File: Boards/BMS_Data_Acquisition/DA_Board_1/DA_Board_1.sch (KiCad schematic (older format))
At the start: 75 parts, among them J1 MM_M_VT_10, J2 MM_M_VT_12, J3 MM_M_VT_12, J4 MM_M_VT_12, J5 MM_M_VT_16, J6 MM_M_VT_10, J7 MM_M_VT_12, J8 MM_M_VT_12, J9 MM_M_VT_12, Q10 BSS308PE, Q12 BSS308PE, Q14 BSS308PE, Q16 BSS308PE, Q2 BSS308PE, Q4 BSS308PE, Q6 BSS308PE, Q8 BSS308PE, T0 Tab_Connect_BMS, T10 Tab_Connect_BMS, T12 Tab_Connect_BMS, T14 Tab_Connect_BMS, T16 Tab_Connect_BMS, T2 Tab_Connect_BMS, T4 Tab_Connect_BMS, T6 Tab_Connect_BMS, T8 Tab_Connect_BMS

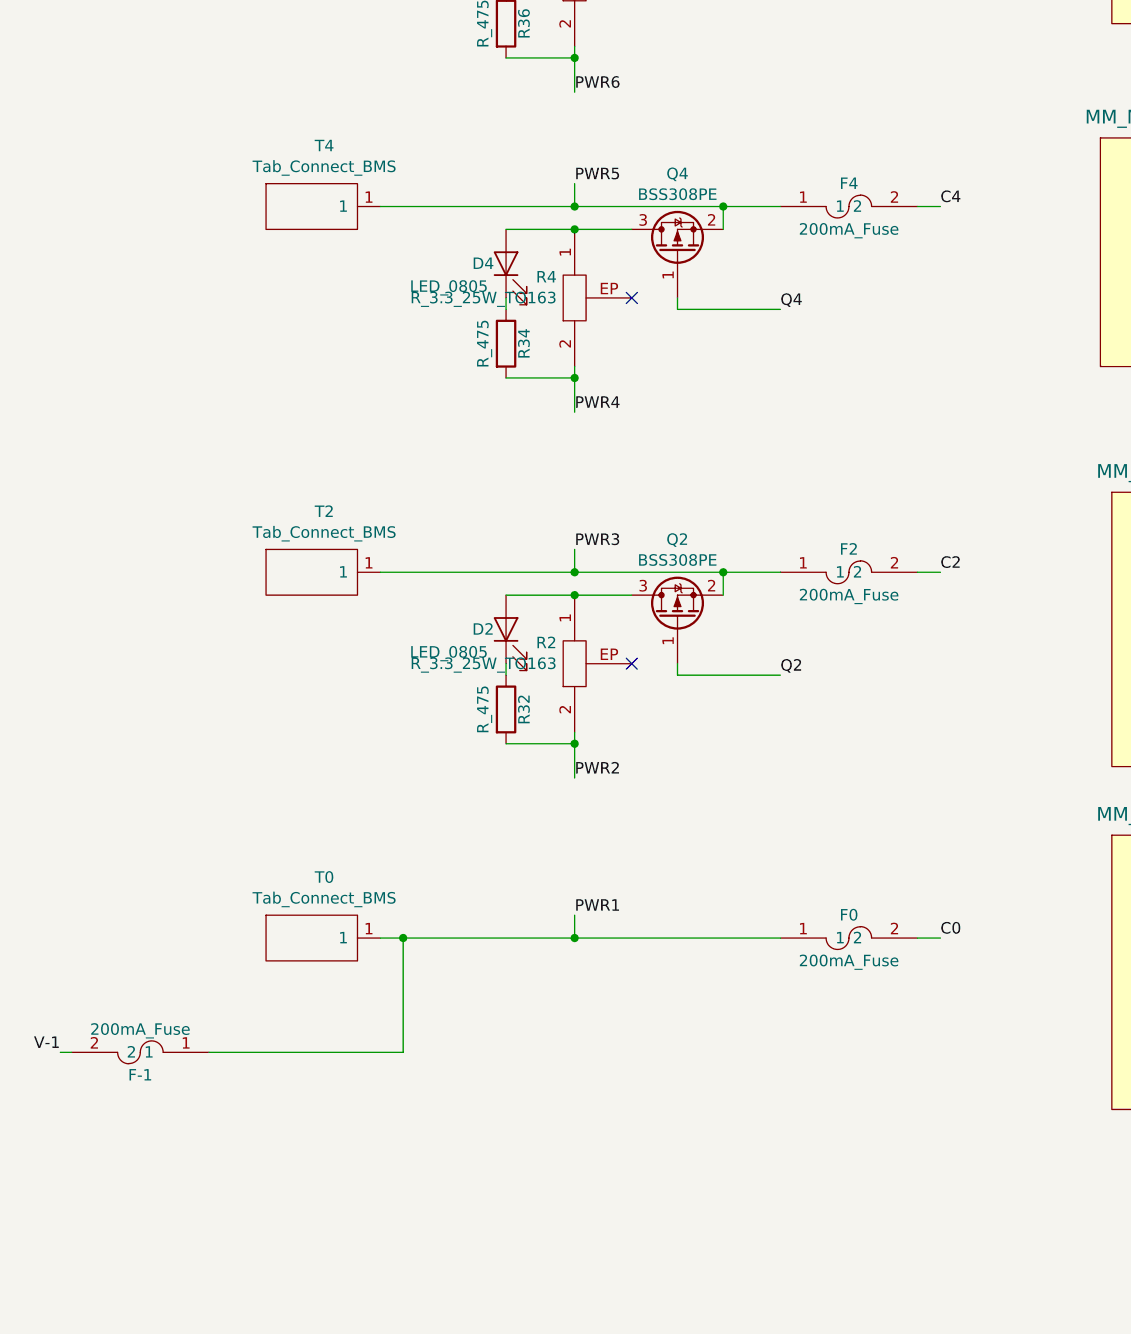
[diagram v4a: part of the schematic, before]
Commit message: adding fuses for balancing circuitry
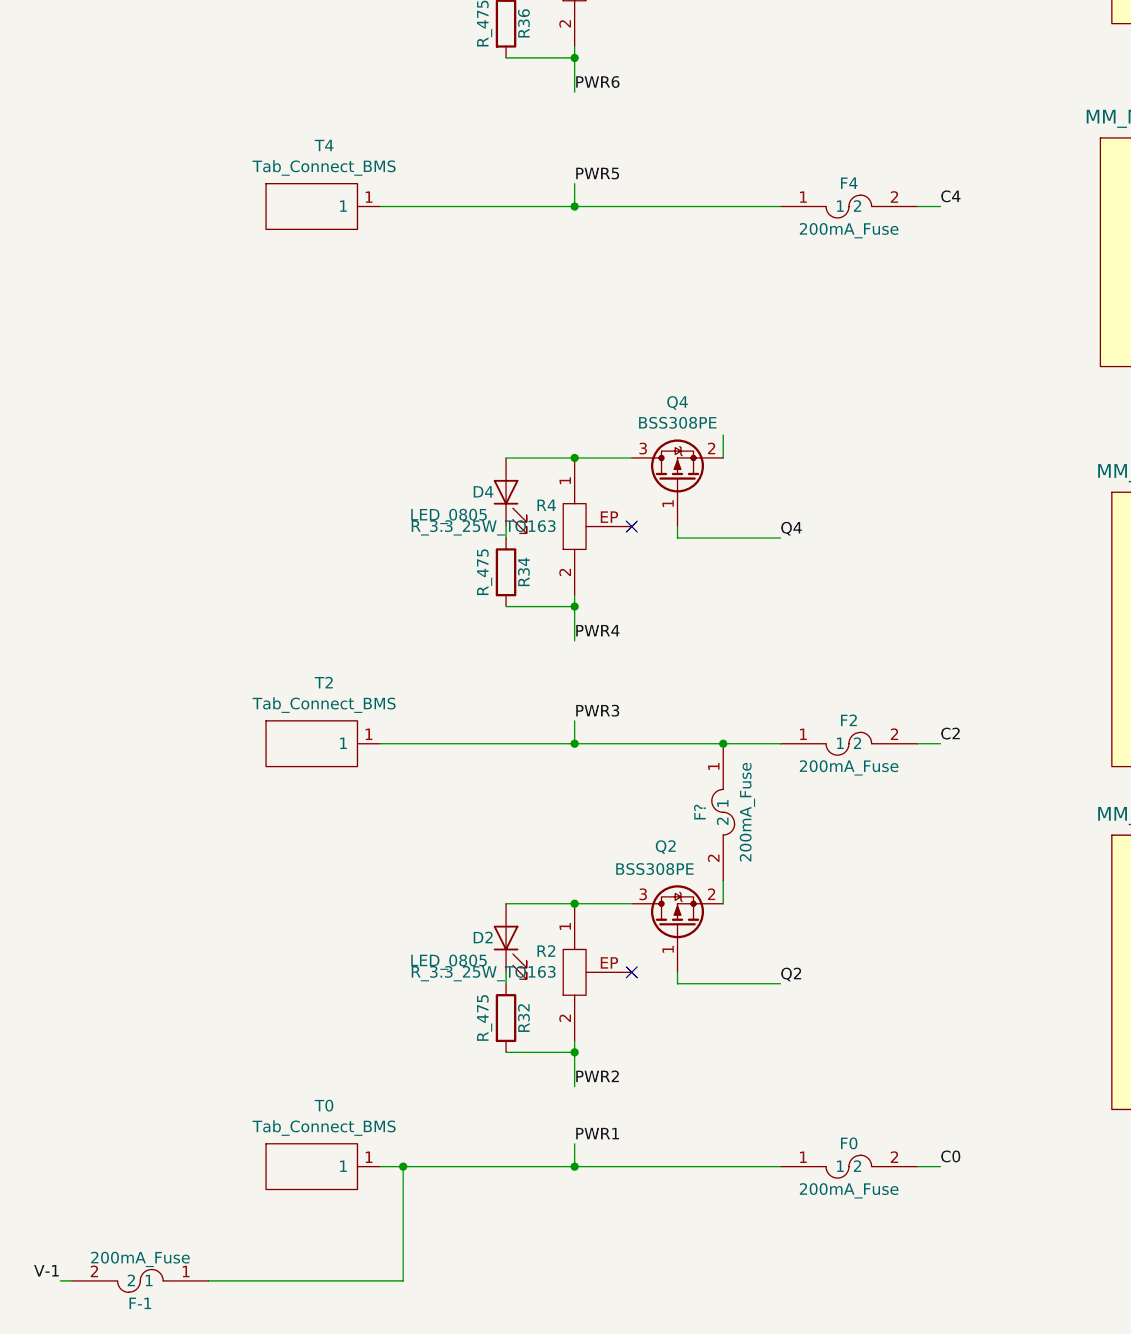
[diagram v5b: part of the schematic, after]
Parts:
- added F?: 200mA_Fuse, footprints:Fuse_1812, symbol formula:200mA_Fuse
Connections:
- net PWR3: now also F?.1; no longer Q2.2 (S)
- net PWR5: no longer Q4.2 (S)
- new net: F?.2, Q2.2 (S)
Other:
- moved on the sheet: D2, D4, F-1, F0, F2, Q2, Q4, R2, R32, R34, R4, T0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
